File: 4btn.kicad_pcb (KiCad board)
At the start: 2 copper layers, 42.5 x 26.3 mm, 38 parts, among them CON1 AVR-ISP, IC1 ATTINY88-A, Q1 2N7002, Q2 2N7002, U1 74HC14D_653, U2 SW_SPST, U3 SW_SPST, U6 SW_SPST, U7 SW_SPST, U8 SCL SCA GND Vcc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

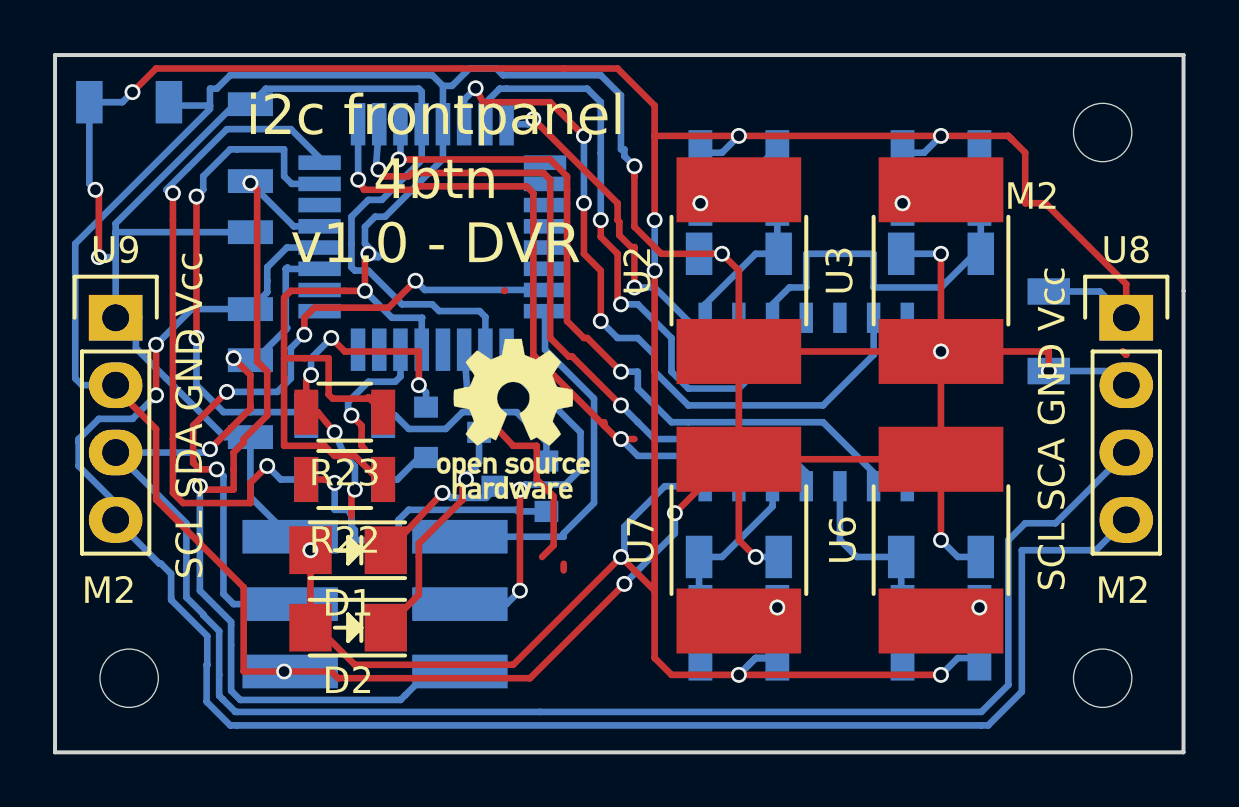
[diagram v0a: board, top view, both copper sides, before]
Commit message: v1.1 fixed 74HC14 bottom-row button pin mappings.
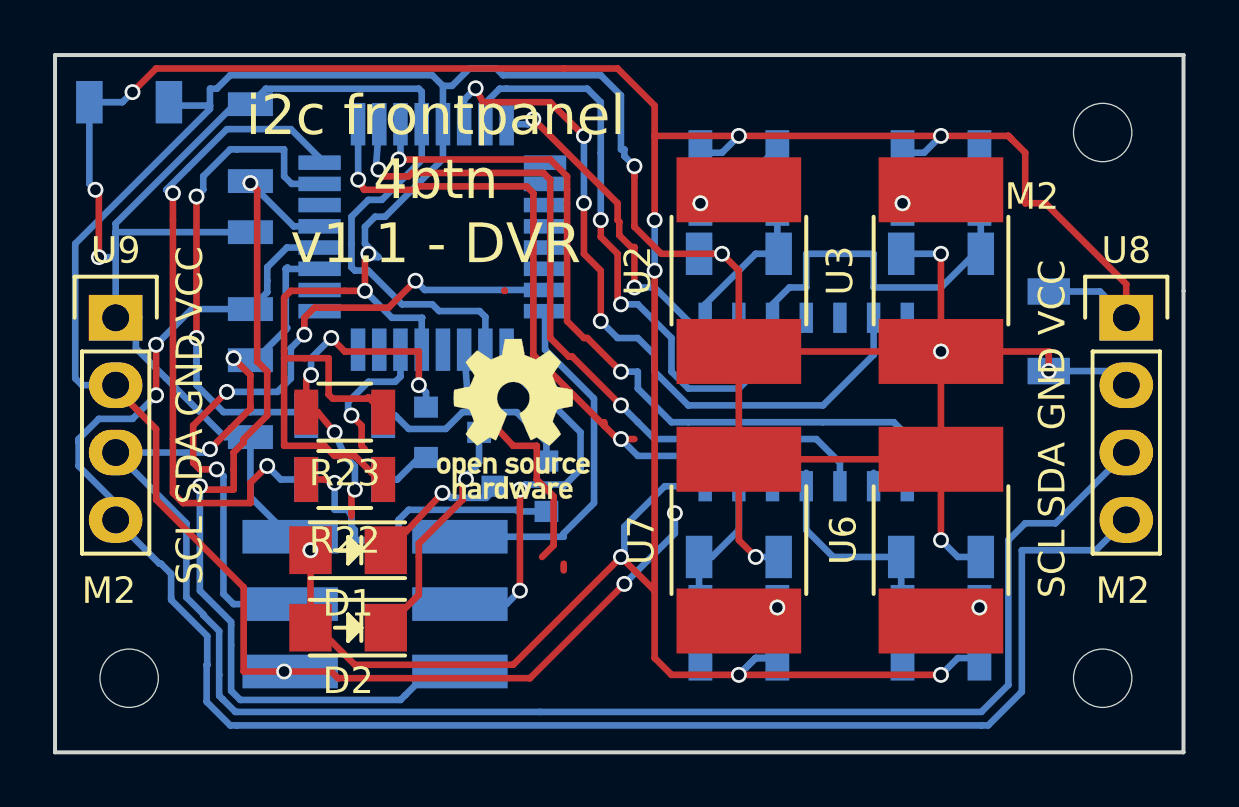
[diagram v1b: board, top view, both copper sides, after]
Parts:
- CON1: value AVR-ISP -> AVR-ISP-6-DR
- U8: value SCL SCA GND Vcc -> SCL SDA GND VCC
- U9: value SCL SDA GND Vcc -> SCL SDA GND VCC
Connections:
- U1 pad 10: /B5 -> /SW5
- U1 pad 11: /SW5 -> /B5
- U1 pad 12: /B6 -> /SW6
- U1 pad 13: /SW6 -> /B6
- U1 pad 8: /B4 -> /SW4
- U1 pad 9: /SW4 -> /B4
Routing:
- net GND: track 163.4 -> 160.5 mm
- net /SW4: track 28.2 -> 30.3 mm
- net /B5: track 6.53 -> 8.09 mm
- net /SW5: track 26.8 -> 28.3 mm
- net /SW6: track 26.0 -> 27.4 mm
- net /B4: track 0.00 -> 0.51 mm
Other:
- board text added: "i2c frontpanel 4btn v1.1 - DVR"
- board text removed: "i2c frontpanel 4btn v1.0 - DVR"
